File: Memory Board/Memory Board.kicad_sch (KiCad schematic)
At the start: 36 parts, among them IC1 W25Q01JVZEIQ, J1 USB_C_Receptacle, J2 Conn_01x04_Socket, J3 Conn_01x04_Socket, J4 Conn_01x04_Socket, SW1 SW_SPST, U1 STM32G473CBTx, U2 LD1117S33TR_SOT223, U3 LD1117S50TR_SOT223, U4 MCP2557FD-xSN, X1 ECS-2520MV-xxx-xx

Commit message: Started on pcb layout
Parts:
- removed J1: USB_C_Receptacle, Connector_USB:USB_C_Plug_Molex_105444, symbol Connector:USB_C_Receptacle
- removed U4: MCP2557FD-xSN, Package_SO:SOIC-8_3.9x4.9mm_P1.27mm, symbol Interface_CAN_LIN:MCP2557FD-xSN
- added H1, H2, H3, H4: MountingHole_Pad, MountingHole:MountingHole_3.2mm_M3_Pad_TopBottom, symbol Mechanical:MountingHole_Pad
- added IC2: MCP2557FDT-H_MNY, MCP2557FDT-H_MNY:SON50P300X200X80-9N-D, symbol MCP2557FDT-H_MNY:MCP2557FDT-H_MNY
- added J1: USB4056-03-A_REVA2, USB4056-03-A:GCT_USB4056-03-A_REVA2, symbol USB4056-03-A:USB4056-03-A_REVA2
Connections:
- net +5V: now also IC2.3 (VDD)
- net CAN_FD_H: now also IC2.7 (CANH)
- net CAN_FD_L: now also IC2.6 (CANL)
- net FDCAN_RX: now also IC2.4 (RXD)
- net FDCAN_TX: now also IC2.1 (TXD)
- net GND: now also H1.1, H2.1, H3.1, H4.1, IC2.2 (VSS), IC2.9 (EP), J1.A1 (GND_A), J1.A12 (GND_A), J1.B1 (GND_B), J1.B12 (GND_B), J1.S1 (SHELL_GND), J1.S2 (SHELL_GND), J1.S3 (SHELL_GND), J1.S4 (SHELL_GND)
- net LED_B: now also U1.32 (PA10)
- net LED_G: now also U1.31 (PA9)
- net LED_R: now also U1.30 (PA8)
- net PWR IN: now also J1.A4 (VBUS_A), J1.A9 (VBUS_A), J1.B4 (VBUS_B), J1.B9 (VBUS_B)
- net TXD: now also U1.39 (PA15), IC2.8 (S)
- net USB_D+: now also J1.A6 (DP1)
- net USB_D-: now also J1.A7 (DN1)
- no-connect marks 15 -> 34
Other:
- moved on the sheet: C15, C16, J3, R5, R6, SW1

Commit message: Layout work
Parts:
- removed J4: Conn_01x04_Socket, Connector_PinHeader_2.54mm:PinHeader_1x04_P2.54mm_Vertical, symbol Connector:Conn_01x04_Socket
- added J4, J5: Conn_01x02_Socket, Connector_PinHeader_2.54mm:PinHeader_1x02_P2.54mm_Vertical, symbol Connector:Conn_01x02_Socket
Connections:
- net +3.3V: now also J5.1 (Pin_1)
- net GND: now also J5.2 (Pin_2)
- net SYS_SWCLK: now also J4.1 (Pin_1)
- net SYS_SWDIO: now also J4.2 (Pin_2)

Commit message: Lab Work
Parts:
- removed C11: .1uF, Capacitor_SMD:C_0402_1005Metric, symbol Device:C
- removed C12: 10uF, Capacitor_SMD:C_0603_1608Metric, symbol Device:C
- removed J4, J5: Conn_01x02_Socket, Connector_PinHeader_2.54mm:PinHeader_1x02_P2.54mm_Vertical, symbol Connector:Conn_01x02_Socket
- removed U3: LD1117S50TR_SOT223, Package_TO_SOT_SMD:SOT-223-3_TabPin2, symbol Regulator_Linear:LD1117S50TR_SOT223
- added J4: Conn_01x04_Socket, Connector_PinHeader_2.54mm:PinHeader_1x04_P2.54mm_Vertical, symbol Connector:Conn_01x04_Socket
- R3, R4, R7: footprint Resistor_SMD:R_0603_1608Metric -> Resistor_SMD:R_0402_1005Metric
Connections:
- net +5V is gone; now on net PWR IN: C15.1, IC2.3 (VDD)
- net +3.3V: now also J4.4 (Pin_4)
- net GND: now also J4.3 (Pin_3)
- net LED_B: now also U1.27 (PB13); no longer U1.32 (PA10)
- net LED_G: now also U1.29 (PB15); no longer U1.31 (PA9)
- net LED_R: now also U1.25 (PB11); no longer U1.30 (PA8)
- net SYS_SWCLK: now also J4.2 (Pin_2)
- net SYS_SWDIO: now also J4.1 (Pin_1)
- net TXD: now also U1.41 (PB4); no longer U1.39 (PA15)
- no-connect marks 34 -> 33
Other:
- note removed: "5.0V Regulator"
- note removed: "Output: 5.0V 800ma Input: 15V Max"

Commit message: Complete board
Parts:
- removed H3, H4: MountingHole_Pad, MountingHole:MountingHole_3.2mm_M3_Pad_TopBottom, symbol Mechanical:MountingHole_Pad
- J1: footprint USB4056-03-A:GCT_USB4056-03-A_REVA2 -> Connector_USB:USB_C_Receptacle_GCT_USB4115-03-C
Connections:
- net CAN_FD_H: now also J3.1 (Pin_1), J3.2 (Pin_2); no longer J3.3 (Pin_3), J3.4 (Pin_4)
- net CAN_FD_L: now also J3.3 (Pin_3), J3.4 (Pin_4); no longer J3.1 (Pin_1), J3.2 (Pin_2)
- net GND: now also J2.1 (Pin_1), J2.2 (Pin_2); no longer J2.3 (Pin_3), J2.4 (Pin_4)
- net LED_G: now also U1.25 (PB11); no longer U1.29 (PB15)
- net LED_R: now also U1.29 (PB15); no longer U1.25 (PB11)
- net PWR IN: now also J2.3 (Pin_3), J2.4 (Pin_4); no longer J2.1 (Pin_1), J2.2 (Pin_2)
- no-connect marks 33 -> 34
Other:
- moved on the sheet: J2

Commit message: Woek
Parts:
- added R8: 10k, Resistor_SMD:R_0402_1005Metric_Pad0.72x0.64mm_HandSolder, symbol Device:R
- added SW2: SW_SPDT, Jumper:SolderJumper-3_P1.3mm_Open_RoundedPad1.0x1.5mm_NumberLabels, symbol Switch:SW_SPDT
- SW1: footprint Jumper:SolderJumper-2_P1.3mm_Open_TrianglePad1.0x1.5mm -> Jumper:SolderJumper-2_P1.3mm_Open_RoundedPad1.0x1.5mm
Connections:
- net +3.3V: now also SW2.3 (C)
- net FDCAN_RX: now also U1.40 (PB3); no longer U1.45 (PB8)
- net FDCAN_TX: now also U1.39 (PA15); no longer U1.46 (PB9)
- net GND: now also SW2.1 (A)
- net TXD: now also U1.42 (PB5); no longer U1.41 (PB4)
- new net: R8.1, SW2.2 (B)
- new net BOOT0: R8.2, U1.45 (PB8)
- no-connect marks 34 -> 33
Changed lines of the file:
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@@
   (no_connect (at 42.545 45.72))
   (no_connect (at 75.565 45.72))
-  (no_connect (at 75.565 63.5))
   (no_connect (at 260.985 139.7))
   (no_connect (at 260.985 129.54))
@@
   (no_connect (at 42.545 48.26))
   (no_connect (at 42.545 43.18))
+  (no_connect (at 42.545 76.2))
   (no_connect (at 225.425 132.08))
   (no_connect (at 42.545 58.42))
@@
   (no_connect (at 75.565 27.94))
   (no_connect (at 260.985 137.16))
+  (no_connect (at 42.545 63.5))
   (no_connect (at 260.985 144.78))
   (no_connect (at 42.545 71.12))
@@
   (no_connect (at 42.545 68.58))
   (no_connect (at 260.985 132.08))
-  (no_connect (at 42.545 60.96))
   (no_connect (at 75.565 48.26))
   (no_connect (at 225.425 144.78))
   (no_connect (at 42.545 83.82))
-  (no_connect (at 42.545 66.04))
   (wire (pts (xy 143.51 80.01) (xy 143.51 78.105))
     (stroke (width 0) (type default))
@@
     (stroke (width 0) (type default))
   )
-  (wire (pts (xy 40.64 76.2) (xy 42.545 76.2))
-    (stroke (width 0) (type default))
-  )
   (wire (pts (xy 122.555 184.785) (xy 123.19 184.785))
     (stroke (width 0) (type default))
@@
     (stroke (width 0) (type default))
   )
-  (wire (pts (xy 40.005 63.5) (xy 42.545 63.5))
-    (stroke (width 0) (type default))
-  )
   (wire (pts (xy 223.52 124.46) (xy 225.425 124.46))
     (stroke (width 0) (type default))
@@
     (stroke (width 0) (type default))
   )
+  (wire (pts (xy 27.305 73.66) (xy 27.94 73.66))
+    (stroke (width 0) (type default))
+  )
   (wire (pts (xy 78.74 53.34) (xy 75.565 53.34))
     (stroke (width 0) (type default))
@@
     (stroke (width 0) (type default))
   )
+  (wire (pts (xy 16.51 71.12) (xy 17.145 71.12))
+    (stroke (width 0) (type default))
+  )
   (wire (pts (xy 21.59 186.69) (xy 23.495 186.69))
     (stroke (width 0) (type default))
@@
     (stroke (width 0) (type default))
   )
+  (wire (pts (xy 17.145 76.2) (xy 16.51 76.2))
+    (stroke (width 0) (type default))
+  )
   (wire (pts (xy 57.785 100.33) (xy 57.785 100.965))
     (stroke (width 0) (type default))
@@
     (stroke (width 0) (type default))
   )
+  (wire (pts (xy 40.005 66.04) (xy 42.545 66.04))
+    (stroke (width 0) (type default))
+  )
   (wire (pts (xy 57.785 19.05) (xy 55.245 19.05))
     (stroke (width 0) (type default))
@@
     (stroke (width 0) (type default))
   )
+  (wire (pts (xy 40.005 60.96) (xy 42.545 60.96))
+    (stroke (width 0) (type default))
+  )
   (wire (pts (xy 208.28 66.04) (xy 208.28 63.5))
     (stroke (width 0) (type default))
@@
     (stroke (width 0) (type default))
   )
+  (wire (pts (xy 78.74 63.5) (xy 75.565 63.5))
+    (stroke (width 0) (type default))
+  )
   (wire (pts (xy 78.105 33.02) (xy 75.565 33.02))
     (stroke (width 0) (type default))
@@
     (stroke (width 0) (type default))
   )
-  (wire (pts (xy 40.64 73.66) (xy 42.545 73.66))
-    (stroke (width 0) (type default))
-  )
   (wire (pts (xy 225.425 147.32) (xy 223.52 147.32))
     (stroke (width 0) (type default))
@@
     (stroke (width 0) (type default))
   )
+  (wire (pts (xy 16.51 76.2) (xy 16.51 76.835))
+    (stroke (width 0) (type default))
+  )
   (wire (pts (xy 39.37 53.34) (xy 42.545 53.34))
     (stroke (width 0) (type default))
@@
     (stroke (width 0) (type default))
   )
+  (wire (pts (xy 16.51 69.85) (xy 16.51 71.12))
+    (stroke (width 0) (type default))
+  )
   (wire (pts (xy 222.885 137.16) (xy 225.425 137.16))
     (stroke (width 0) (type default))
@@
   )
   (wire (pts (xy 265.43 26.035) (xy 262.89 26.035))
+    (stroke (width 0) (type default))
+  )
+  (wire (pts (xy 35.56 73.66) (xy 42.545 73.66))
     (stroke (width 0) (type default))
   )
@@
   (text "VDDA" (at 128.27 58.42 0)
     (effects (font (size 2 2) (thickness 0.4) bold) (justify right bottom))
+  )
+  (label "BOOT0" (at 35.56 73.66 0) (fields_autoplaced)
+    (effects (font (size 1.27 1.27)) (justify left bottom))
   )
   (global_label "LED_R" (shape input) (at 40.64 91.44 180) (fields_autoplaced)
@@
     )
   )
-  (global_label "FDCAN_RX" (shape input) (at 40.64 73.66 180) (fields_autoplaced)
+  (global_label "FDCAN_RX" (shape input) (at 40.005 60.96 180) (fields_autoplaced)
     (effects (font (size 1.27 1.27)) (justify right))
-    (property "Intersheetrefs" "${INTERSHEET_REFS}" (at 28.16 73.66 0)
+    (property "Intersheetrefs" "${INTERSHEET_REFS}" (at 27.525 60.96 0)
       (effects (font (size 1.27 1.27)) (justify right) hide)
     )
@@
     )
   )
-  (global_label "TXD" (shape input) (at 40.005 63.5 180) (fields_autoplaced)
+  (global_label "TXD" (shape input) (at 40.005 66.04 180) (fields_autoplaced)
     (effects (font (size 1.27 1.27)) (justify right))
-    (property "Intersheetrefs" "${INTERSHEET_REFS}" (at 33.5727 63.5 0)
+    (property "Intersheetrefs" "${INTERSHEET_REFS}" (at 33.5727 66.04 0)
       (effects (font (size 1.27 1.27)) (justify right) hide)
     )
@@
     )
   )
-  (global_label "FDCAN_TX" (shape input) (at 40.64 76.2 180) (fields_autoplaced)
-    (effects (font (size 1.27 1.27)) (justify right))
-    (property "Intersheetrefs" "${INTERSHEET_REFS}" (at 28.4624 76.2 0)
-      (effects (font (size 1.27 1.27)) (justify right) hide)
+  (global_label "FDCAN_TX" (shape input) (at 78.74 63.5 0) (fields_autoplaced)
+    (effects (font (size 1.27 1.27)) (justify left))
+    (property "Intersheetrefs" "${INTERSHEET_REFS}" (at 90.9176 63.5 0)
+      (effects (font (size 1.27 1.27)) (justify left) hide)
     )
   )
@@
     )
   )
+  (symbol (lib_id "power:GND") (at 16.51 76.835 0) (unit 1)
+    (in_bom yes) (on_board yes) (dnp no) (fields_autoplaced)
+    (property "Reference" "#PWR04" (at 16.51 83.185 0)
+      (effects (font (size 1.27 1.27)) hide)
+    )
+    (property "Value" "GND" (at 16.51 81.28 0)
+      (effects (font (size 1.27 1.27)) hide)
+    )
+    (property "Footprint" "" (at 16.51 76.835 0)
+      (effects (font (size 1.27 1.27)) hide)
+    )
+    (property "Datasheet" "" (at 16.51 76.835 0)
+      (effects (font (size 1.27 1.27)) hide)
+    )
+    (pin "1")
+    (instances
+      (project "Memory Board"
+        (path "/72e2bc66-4627-403e-9108-ec8db4d305b2"
+          (reference "#PWR04") (unit 1)
+        )
+      )
+    )
+  )
   (symbol (lib_id "power:GND") (at 241.3 103.505 0) (unit 1)
     (in_bom yes) (on_board yes) (dnp no) (fields_autoplaced)
@@
         (path "/72e2bc66-4627-403e-9108-ec8db4d305b2"
           (reference "#PWR024") (unit 1)
+        )
+      )
+    )
+  )
+  (symbol (lib_id "power:+3.3V") (at 16.51 69.85 0) (unit 1)
+    (in_bom yes) (on_board yes) (dnp no) (fields_autoplaced)
+    (property "Reference" "#PWR013" (at 16.51 73.66 0)
+      (effects (font (size 1.27 1.27)) hide)
+    )
+    (property "Value" "+3.3V" (at 16.51 65.405 0)
+      (effects (font (size 1.27 1.27)))
+    )
+    (property "Footprint" "" (at 16.51 69.85 0)
+      (effects (font (size 1.27 1.27)) hide)
+    )
+    (property "Datasheet" "" (at 16.51 69.85 0)
+      (effects (font (size 1.27 1.27)) hide)
+    )
+    (pin "1")
+    (instances
+      (project "Memory Board"
+        (path "/72e2bc66-4627-403e-9108-ec8db4d305b2"
+          (reference "#PWR013") (unit 1)
         )
       )
@@
     )
   )
+  (symbol (lib_id "Switch:SW_SPDT") (at 22.225 73.66 180) (unit 1)
+    (in_bom yes) (on_board yes) (dnp no)
+    (property "Reference" "SW2" (at 23.495 70.485 0)
+      (effects (font (size 1.27 1.27)))
+    )
+    (property "Value" "SW_SPDT" (at 23.495 77.47 0)
+      (effects (font (size 1.27 1.27)))
+    )
+    (property "Footprint" "Jumper:SolderJumper-3_P1.3mm_Open_RoundedPad1.0x1.5mm_NumberLabels" (at 22.225 73.66 0)
+      (effects (font (size 1.27 1.27)) hide)
+    )
+    (property "Datasheet" "~" (at 22.225 73.66 0)
+      (effects (font (size 1.27 1.27)) hide)
+    )
+    (pin "1")
+    (pin "2")
+    (pin "3")
+    (instances
+      (project "Memory Board"
+        (path "/72e2bc66-4627-403e-9108-ec8db4d305b2"
+          (reference "SW2") (unit 1)
+        )
+      )
+    )
+  )
   (symbol (lib_id "power:GND") (at 114.3 54.61 0) (unit 1)
     (in_bom yes) (on_board yes) (dnp no) (fields_autoplaced)
@@
         (path "/72e2bc66-4627-403e-9108-ec8db4d305b2"
           (reference "J3") (unit 1)
+        )
+      )
+    )
+  )
+  (symbol (lib_id "Device:R") (at 31.75 73.66 90) (unit 1)
+    (in_bom yes) (on_board yes) (dnp no) (fields_autoplaced)
+    (property "Reference" "R8" (at 31.75 67.31 90)
+      (effects (font (size 1.27 1.27)))
+    )
+    (property "Value" "10k" (at 31.75 69.85 90)
+      (effects (font (size 1.27 1.27)))
+    )
+    (property "Footprint" "Resistor_SMD:R_0402_1005Metric_Pad0.72x0.64mm_HandSolder" (at 31.75 75.438 90)
+      (effects (font (size 1.27 1.27)) hide)
+    )
+    (property "Datasheet" "~" (at 31.75 73.66 0)
+      (effects (font (size 1.27 1.27)) hide)
+    )
+    (pin "1")
+    (pin "2")
+    (instances
+      (project "Memory Board"
+        (path "/72e2bc66-4627-403e-9108-ec8db4d305b2"
+          (reference "R8") (unit 1)
         )
       )
@@
       (effects (font (size 1.27 1.27)) (justify left))
     )
-    (property "Footprint" "Jumper:SolderJumper-2_P1.3mm_Open_TrianglePad1.0x1.5mm" (at 265.43 68.58 0)
-      (effects (font (size 1.27 1.27)) hide)
-    )
+    (property "Footprint" "Jumper:SolderJumper-2_P1.3mm_Open_RoundedPad1.0x1.5mm" (at 265.43 68.58 0)
+      (effects (font (size 1.27 1.27)) hide)
+    )

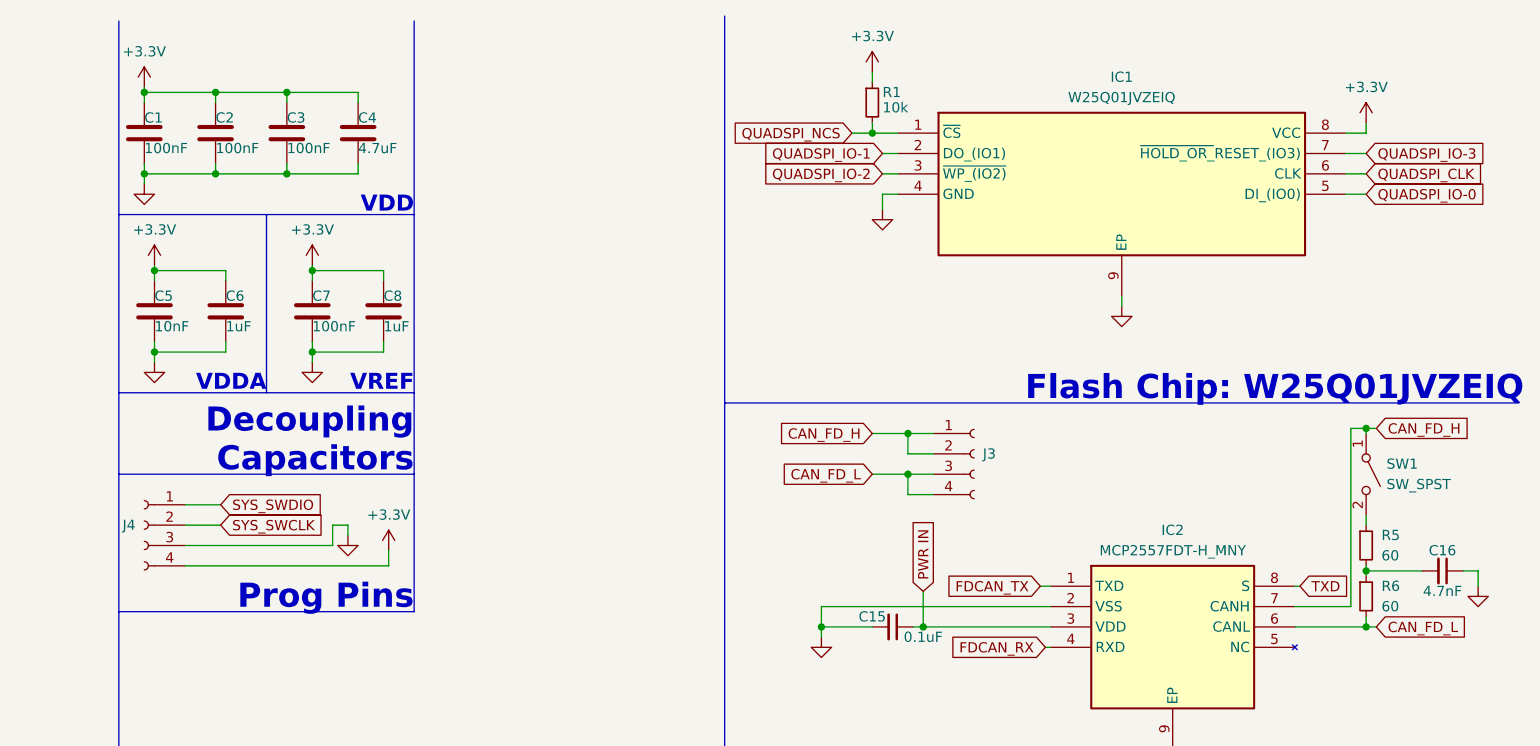
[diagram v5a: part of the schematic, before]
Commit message: Revised good mems
https://www.digikey.com/short/14vp1r7m
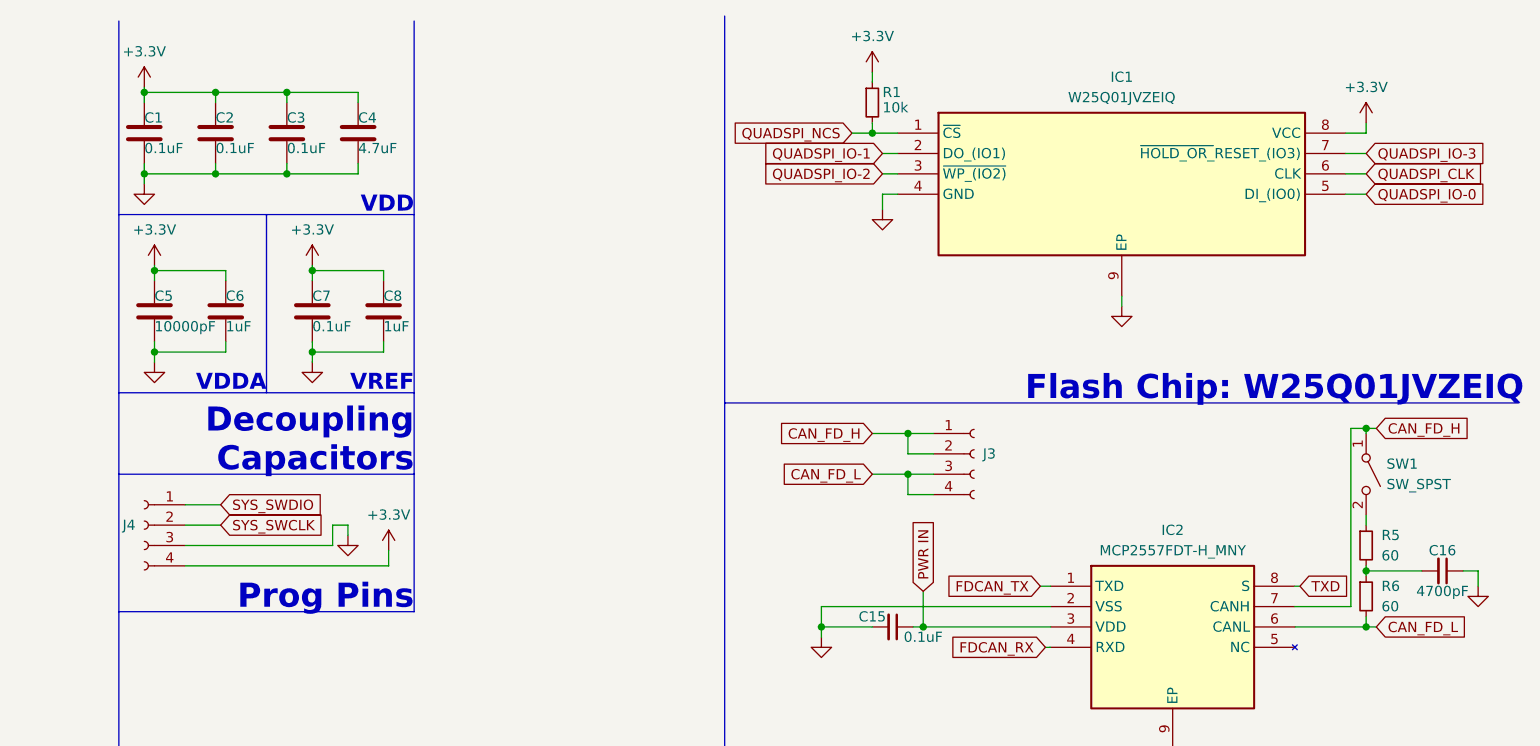
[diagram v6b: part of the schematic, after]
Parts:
- C1, C2, C3, C7: value 100nF -> 0.1uF
- C16: value 4.7nF -> 4700pF
- C5: value 10nF -> 10000pF
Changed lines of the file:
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@@
       (effects (font (size 1.27 1.27)) (justify left))
     )
-    (property "Value" "10nF" (at 114.3 50.165 0)
+    (property "Value" "10000pF" (at 114.3 50.165 0)
       (effects (font (size 1.27 1.27)) (justify left))
     )
@@
       (effects (font (size 1.27 1.27)) (justify left))
     )
-    (property "Value" "100nF" (at 121.92 27.94 0)
+    (property "Value" "0.1uF" (at 121.92 27.94 0)
       (effects (font (size 1.27 1.27)) (justify left))
     )
@@
       (effects (font (size 1.27 1.27)))
     )
-    (property "Value" "4.7nF" (at 274.955 83.185 90)
+    (property "Value" "4700pF " (at 274.955 83.185 90)
       (effects (font (size 1.27 1.27)))
     )
@@
       (effects (font (size 1.27 1.27)) (justify left))
     )
-    (property "Value" "100nF" (at 133.985 50.165 0)
+    (property "Value" "0.1uF" (at 133.985 50.165 0)
       (effects (font (size 1.27 1.27)) (justify left))
     )
@@
       (effects (font (size 1.27 1.27)) (justify left))
     )
-    (property "Value" "100nF" (at 130.81 27.94 0)
+    (property "Value" "0.1uF" (at 130.81 27.94 0)
       (effects (font (size 1.27 1.27)) (justify left))
     )
@@
       (effects (font (size 1.27 1.27)) (justify left))
     )
-    (property "Value" "100nF" (at 113.03 27.94 0)
-      (effects (font (size 1.27 1.27)) (justify left))
-    )
+    (property "Value" "0.1uF" (at 113.03 27.94 0)
+      (effects (font (size 1.27 1.27)) (justify left))
+    )
